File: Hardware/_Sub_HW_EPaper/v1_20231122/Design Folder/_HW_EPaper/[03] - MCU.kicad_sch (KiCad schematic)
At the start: 7 parts, among them J301 HDR_4POS_VERT, U301 PIC16F15223_8BIT

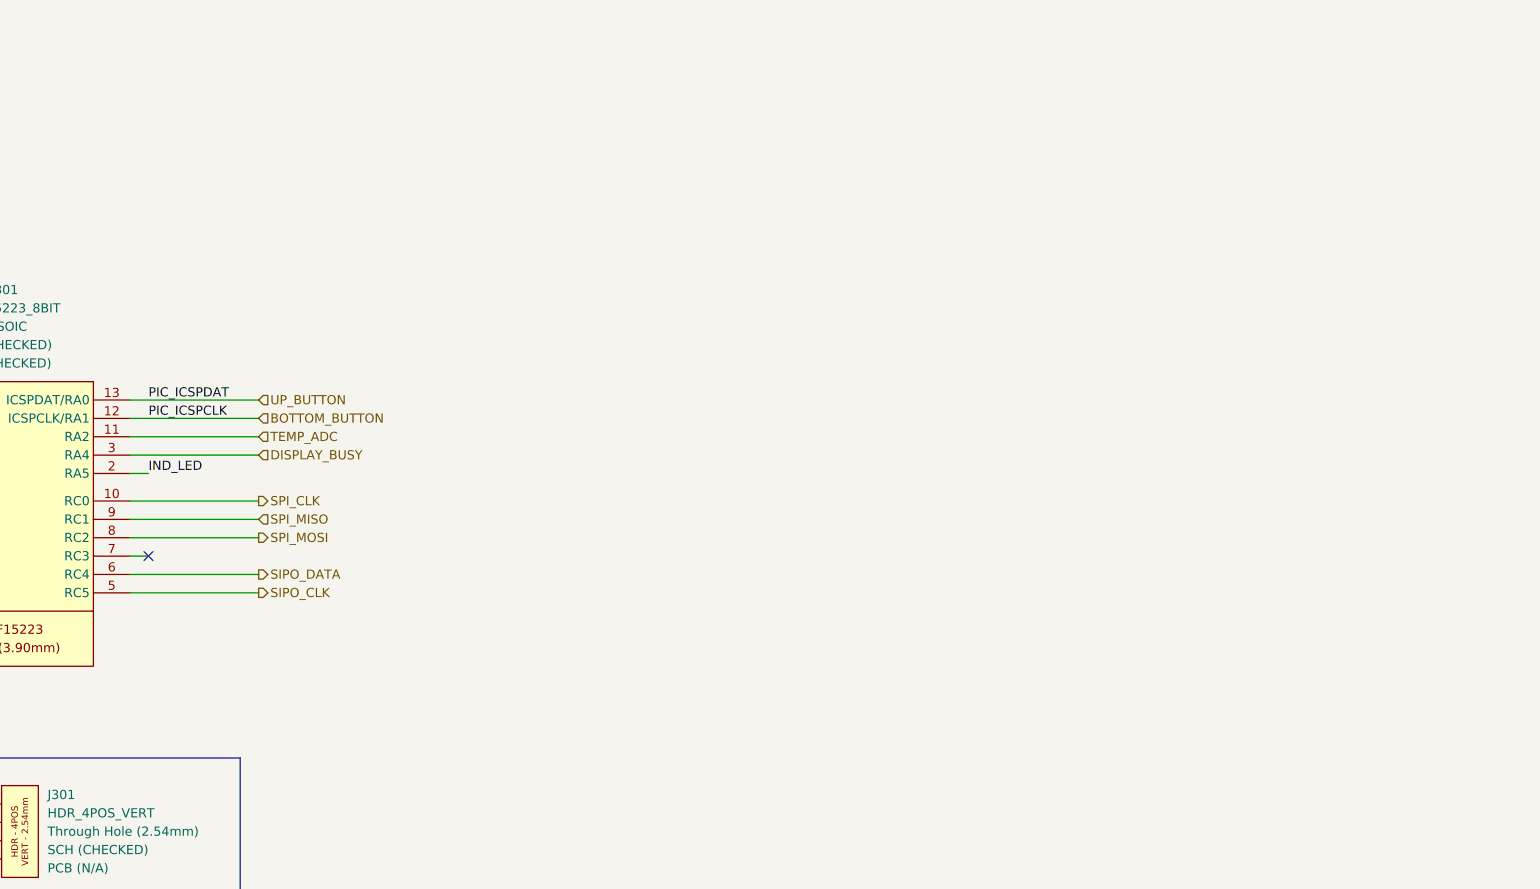
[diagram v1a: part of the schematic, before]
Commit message: Working on epaper hardware
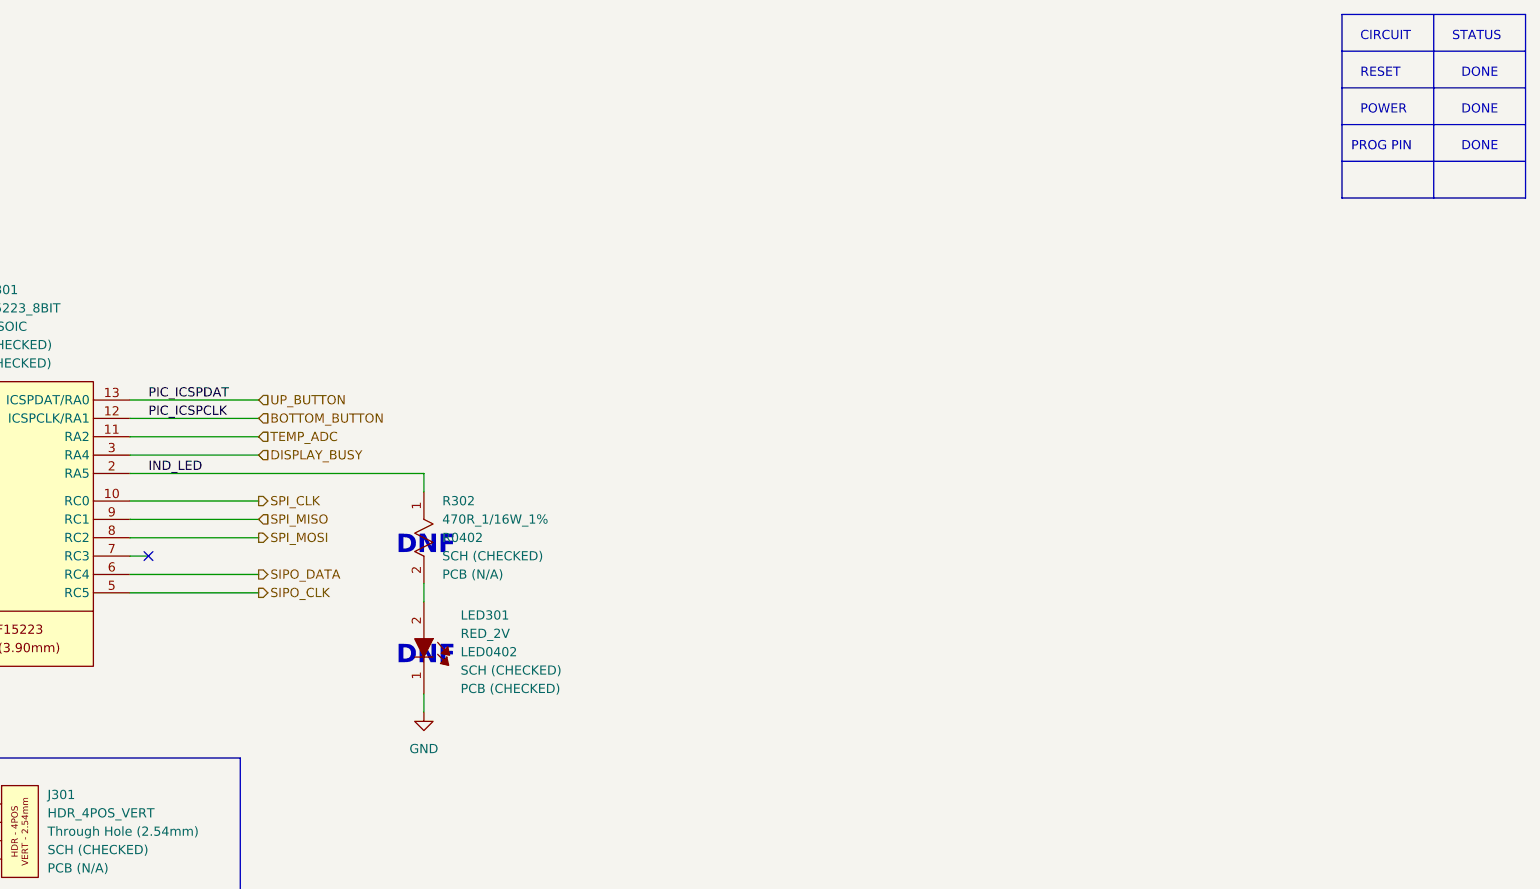
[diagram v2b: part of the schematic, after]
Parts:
- added LED301: RED_2V, LED_SMD:LED_0402_1005Metric, symbol _SCHLIB_Epaper:LED_RED_2V_624nm_LED0402
- added R302: 470R_1/16W_1%, Resistor_SMD:R_0402_1005Metric, symbol _SCHLIB_Epaper:RES_470R_1/16W_1%_R0402
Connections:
- net GND: now also LED301.1
- net IND_LED: now also R302.1
- new net: LED301.2, R302.2
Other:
- note added: "CIRCUIT"
- note added: "DNF"
- note added: "DONE"
- note added: "POWER"
- note added: "PROG PIN"
- note added: "RESET"
- note added: "STATUS"
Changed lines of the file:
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@@
     (company "Mend0z0")
     (comment 1 "v1.0")
-    (comment 2 "PRELIMINARY")
+    (comment 2 "CHECKED")
   )
   (junction (at 135.89 128.27) (diameter 0) (color 0 0 0 0)
@@
     (stroke (width 0) (type default))
   )
+  (wire (pts (xy 254 129.54) (xy 254 132.08))
+    (stroke (width 0) (type default))
+  )
   (wire (pts (xy 156.21 128.27) (xy 156.21 130.81))
     (stroke (width 0) (type default))
@@
     (stroke (width 0) (type default))
   )
+  (polyline (pts (xy 381 60.96) (xy 406.4 60.96))
+    (stroke (width 0) (type default))
+  )
   (wire (pts (xy 135.89 102.87) (xy 135.89 104.14))
     (stroke (width 0) (type default))
@@
     (stroke (width 0) (type default))
   )
+  (polyline (pts (xy 393.7 50.8) (xy 393.7 76.2))
+    (stroke (width 0) (type default))
+  )
   (wire (pts (xy 213.36 106.68) (xy 231.14 106.68))
     (stroke (width 0) (type default))
   )
-  (wire (pts (xy 213.36 114.3) (xy 215.9 114.3))
+  (wire (pts (xy 213.36 114.3) (xy 254 114.3))
     (stroke (width 0) (type default))
   )
@@
     (stroke (width 0) (type default))
   )
+  (polyline (pts (xy 381 55.88) (xy 406.4 55.88))
+    (stroke (width 0) (type default))
+  )
   (wire (pts (xy 135.89 130.81) (xy 135.89 128.27))
     (stroke (width 0) (type default))
@@
     (stroke (width 0) (type default))
   )
+  (wire (pts (xy 254 147.32) (xy 254 144.78))
+    (stroke (width 0) (type default))
+  )
   (wire (pts (xy 231.14 130.81) (xy 213.36 130.81))
     (stroke (width 0) (type default))
@@
     (stroke (width 0) (type default))
   )
+  (wire (pts (xy 254 116.84) (xy 254 114.3))
+    (stroke (width 0) (type default))
+  )
   (wire (pts (xy 177.8 130.81) (xy 175.26 130.81))
     (stroke (width 0) (type default))
@@
     (stroke (width 0) (type default))
   )
+  (polyline (pts (xy 381 71.12) (xy 406.4 71.12))
+    (stroke (width 0) (type default))
+  )
   (polyline (pts (xy 109.22 140.97) (xy 134.62 129.54))
     (stroke (width 0) (type default))
@@
     (stroke (width 0) (type default))
   )
+  (polyline (pts (xy 381 66.04) (xy 406.4 66.04))
+    (stroke (width 0) (type default))
+  )
   (rectangle (start 69.85 99.06) (end 110.49 110.49)
     (stroke (width 0) (type default))
     (fill (type none))
   )
+  (rectangle (start 381 50.8) (end 406.4 76.2)
+    (stroke (width 0) (type default))
+    (fill (type none))
+  )
   (circle (center 135.89 128.27) (radius 1.27)
     (stroke (width 0) (type default))
@@
   )
   (text "HPF1" (at 137.16 127 0)
+    (effects (font (size 1.27 1.27)) (justify left bottom))
+  )
+  (text "RESET" (at 383.54 59.69 0)
+    (effects (font (size 1.27 1.27)) (justify left bottom))
+  )
+  (text "DNF" (at 250.19 125.73 0)
+    (effects (font (size 2.54 2.54) (thickness 0.508) bold) (justify left bottom))
+  )
+  (text "DONE" (at 397.51 64.77 0)
     (effects (font (size 1.27 1.27)) (justify left bottom))
   )
@@
     (effects (font (size 2 2) (thickness 0.4) bold) (justify left bottom))
   )
+  (text "PROG PIN" (at 382.27 69.85 0)
+    (effects (font (size 1.27 1.27)) (justify left bottom))
+  )
+  (text "POWER" (at 383.54 64.77 0)
+    (effects (font (size 1.27 1.27)) (justify left bottom))
+  )
+  (text "DONE" (at 397.51 59.69 0)
+    (effects (font (size 1.27 1.27)) (justify left bottom))
+  )
+  (text "DONE" (at 397.51 69.85 0)
+    (effects (font (size 1.27 1.27)) (justify left bottom))
+  )
   (text "HPF: 1/(10*10^3 * 1*10^-6) = 1 kHz" (at 71.12 107.95 0)
     (effects (font (size 1.27 1.27)) (justify left bottom))
@@
     (effects (font (size 1.27 1.27)) (justify left bottom))
   )
+  (text "DNF" (at 250.19 140.97 0)
+    (effects (font (size 2.54 2.54) (thickness 0.508) bold) (justify left bottom))
+  )
+  (text "STATUS" (at 396.24 54.61 0)
+    (effects (font (size 1.27 1.27)) (justify left bottom))
+  )
   (text "PROGRAMMER PINS\n\n" (at 179.07 181.61 0)
     (effects (font (size 2.54 2.54)) (justify left bottom))
   )
+  (text "CIRCUIT" (at 383.54 54.61 0)
+    (effects (font (size 1.27 1.27)) (justify left bottom))
+  )
   (label "PIC_ICSPDAT" (at 176.53 165.1 0) (fields_autoplaced)
     (effects (font (size 1.27 1.27)) (justify left bottom))
@@
   (hierarchical_label "VIN" (shape input) (at 133.35 87.63 180) (fields_autoplaced)
     (effects (font (size 1.27 1.27)) (justify right))
+  )
+  (symbol (lib_id "_SCHLIB_Epaper:RES_470R_1/16W_1%_R0402") (at 254 116.84 270) (unit 1)
+    (in_bom yes) (on_board yes) (dnp no) (fields_autoplaced)
+    (property "Reference" "R302" (at 256.54 118.11 90)
+      (effects (font (size 1.27 1.27)) (justify left))
+    )
+    (property "Value" "470R_1/16W_1%" (at 256.54 120.65 90)
+      (effects (font (size 1.27 1.27)) (justify left))
+    )
+    (property "Footprint" "Resistor_SMD:R_0402_1005Metric" (at 270.51 119.38 0)
+      (effects (font (size 1.27 1.27)) (justify left) hide)
+    )
+    (property "Datasheet" "https://www.bourns.com/docs/product-datasheets/cr.pdf?sfvrsn=574d41f6_14" (at 262.89 119.38 0)
+      (effects (font (size 1.27 1.27)) (justify left) hide)
+    )
+    (property "Description" "470 Ohms ±1% 0.063W, 1/16W Chip Resistor 0402 (1005 Metric) Thick Film" (at 267.97 119.38 0)
+      (effects (font (size 1.27 1.27)) (justify left) hide)
+    )
+    (property "Part Number" "CR0402-FX-4700GLF" (at 273.05 119.38 0)
+      (effects (font (size 1.27 1.27)) (justify left) hide)
+    )
+    (property "Link" "https://www.digikey.ca/en/products/detail/bourns-inc/CR0402-FX-4700GLF/3783391" (at 265.43 119.38 0)
+      (effects (font (size 1.27 1.27)) (justify left) hide)
+    )
+    (property "Package" "R0402" (at 256.54 123.19 90)
+      (effects (font (size 1.27 1.27)) (justify left))
+    )
+    (property "SCH CHECK" "SCH (CHECKED)" (at 256.54 125.73 90)
+      (effects (font (size 1.27 1.27)) (justify left))
+    )
+    (property "PCB CHECK" "PCB (N/A)" (at 256.54 128.27 90)
+      (effects (font (size 1.27 1.27)) (justify left))
+    )
+    (pin "1")
+    (pin "2")
+    (instances
+      (project "_HW_EPaper"
+        (path "/adfaa0ae-c952-44c7-bc24-1bfe8f9a84a3/4e346fc8-747a-4f3e-83e0-81c9211edb38/99cad234-6d2d-4b92-87e6-f4f0e962eb13"
+          (reference "R302") (unit 1)
+        )
+      )
+    )
   )
   (symbol (lib_id "_SCHLIB_Epaper:MCU_PIC16F15223-E/SL_8BIT_14-SOIC") (at 182.88 101.6 0) (unit 1)
@@
     )
   )
+  (symbol (lib_id "power:GND") (at 254 147.32 0) (unit 1)
+    (in_bom yes) (on_board yes) (dnp no) (fields_autoplaced)
+    (property "Reference" "#PWR0302" (at 254 153.67 0)
+      (effects (font (size 1.27 1.27)) hide)
+    )
+    (property "Value" "GND" (at 254 152.4 0)
+      (effects (font (size 1.27 1.27)))
+    )
+    (property "Footprint" "" (at 254 147.32 0)
+      (effects (font (size 1.27 1.27)) hide)
+    )
+    (property "Datasheet" "" (at 254 147.32 0)
+      (effects (font (size 1.27 1.27)) hide)
+    )
+    (pin "1")
+    (instances
+      (project "[03] - MCU"
+        (path "/9bbd5852-431d-48c8-bae6-0765e432421a"
+          (reference "#PWR0302") (unit 1)
+        )
+      )
+      (project "_HW_EPen"
+        (path "/9ee621ae-6984-4881-898c-f5f3c9433407/7dba9ac4-cfde-4903-b774-f23f20ffdff2/4f69a756-13f1-41da-a917-ef791025fd7a"
+          (reference "#PWR0302") (unit 1)
+        )
+      )
+      (project "_HW_EPaper"
+        (path "/adfaa0ae-c952-44c7-bc24-1bfe8f9a84a3/4e346fc8-747a-4f3e-83e0-81c9211edb38/99cad234-6d2d-4b92-87e6-f4f0e962eb13"
+          (reference "#PWR0303") (unit 1)
+        )
+      )
+    )
+  )
+  (symbol (lib_id "_SCHLIB_Epaper:LED_RED_2V_624nm_LED0402") (at 254 132.08 270) (unit 1)
+    (in_bom yes) (on_board yes) (dnp no) (fields_autoplaced)
+    (property "Reference" "LED301" (at 259.08 133.9215 90)
+      (effects (font (size 1.27 1.27)) (justify left))
+    )
+    (property "Value" "RED_2V" (at 259.08 136.4615 90)
+      (effects (font (size 1.27 1.27)) (justify left))
+    )
+    (property "Footprint" "LED_SMD:LED_0402_1005Metric" (at 273.05 134.62 0)
+      (effects (font (size 1.27 1.27)) (justify left) hide)
+    )
+    (property "Datasheet" "https://media.digikey.com/pdf/Data%20Sheets/Harvatek%20PDFs/B2841USD-20D001014U1930.pdf" (at 265.43 134.62 0)
+      (effects (font (size 1.27 1.27)) (justify left) hide)
+    )
+    (property "Description" "Red 624nm LED Indication - Discrete 2V 0402 (1005 Metric)" (at 270.51 134.62 0)
+      (effects (font (size 1.27 1.27)) (justify left) hide)
+    )
+    (property "Part Number" "B2841USD-20D001014U1930" (at 275.59 134.62 0)
+      (effects (font (size 1.27 1.27)) (justify left) hide)
+    )
+    (property "Link" "https://www.digikey.ca/en/products/detail/harvatek-corporation/B2841USD-20D001014U1930/16729514?s=N4IgTCBcDaIEJgBwBYCMBVAygEQLRgAZsCDVTl1UBOAZgJAF0BfIA" (at 267.97 134.62 0)
+      (effects (font (size 1.27 1.27)) (justify left) hide)
+    )
+    (property "Package" "LED0402" (at 259.08 139.0015 90)
+      (effects (font (size 1.27 1.27)) (justify left))
+    )
+    (property "SCH CHECK" "SCH (CHECKED)" (at 259.08 141.5415 90)
+      (effects (font (size 1.27 1.27)) (justify left))
+    )
+    (property "PCB CHECK" "PCB (CHECKED)" (at 259.08 144.0815 90)
+      (effects (font (size 1.27 1.27)) (justify left))
+    )
+    (pin "2")
+    (pin "1")
+    (instances
+      (project "_HW_EPaper"
+        (path "/adfaa0ae-c952-44c7-bc24-1bfe8f9a84a3/4e346fc8-747a-4f3e-83e0-81c9211edb38/99cad234-6d2d-4b92-87e6-f4f0e962eb13"
+          (reference "LED301") (unit 1)
+        )
+      )
+    )
+  )
   (symbol (lib_id "_SCHLIB_Epaper:CAP_100nF_50V_X7R_C0402") (at 156.21 130.81 270) (unit 1)
     (in_bom yes) (on_board yes) (dnp no) (fields_autoplaced)
@@
       (project "_HW_EPaper"
         (path "/adfaa0ae-c952-44c7-bc24-1bfe8f9a84a3/4e346fc8-747a-4f3e-83e0-81c9211edb38/99cad234-6d2d-4b92-87e6-f4f0e962eb13"
-          (reference "R304") (unit 1)
-        )
-      )
+          (reference "R303") (unit 1)
+        )
+      )

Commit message: Updating file templates and structures...
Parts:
- C301, C303: Manufacturer (none) -> Murata Electronics; Part Number GRM155R71H104KE14J -> (none); Part Number (Manufacturer) (none) -> GRM155R71H104KE14J; Part Number (Vendor) (none) -> 490-13342-2-ND; Vendor (none) -> Digikey
- C302: Manufacturer (none) -> Murata Electronics; Part Number GRM155Z71A105KE01D -> (none); Part Number (Manufacturer) (none) -> GRM155Z71A105KE01D; Part Number (Vendor) (none) -> 490-GRM155Z71A105KE01DTR-ND; Vendor (none) -> Digikey
- J301: Manufacturer (none) -> Adam Tech; Part Number PH1-04-UA -> (none); Part Number (Manufacturer) (none) -> PH1-04-UA; Part Number (Vendor) (none) -> 2057-PH1-04-UA-ND; Vendor (none) -> Digikey
- LED301: Manufacturer (none) -> Harvatek Corporation; Part Number B2841USD-20D001014U1930 -> (none); Part Number (Manufacturer) (none) -> B2841USD-20D001014U1930; Part Number (Vendor) (none) -> 3147-B2841USD-20D001014U1930TR-ND; Vendor (none) -> Digikey
- R301: Manufacturer (none) -> Bourns Inc.; Part Number CR0402-FX-1002GLF -> (none); Part Number (Manufacturer) (none) -> CR0402-FX-1002GLF; Part Number (Vendor) (none) -> CR0402-FX-1002GLFTR-ND; Vendor (none) -> Digikey
- R302: Manufacturer (none) -> Bourns Inc.; Part Number CR0402-FX-4700GLF -> (none); Part Number (Manufacturer) (none) -> CR0402-FX-4700GLF; Part Number (Vendor) (none) -> CR0402-FX-4700GLFTR-ND; Vendor (none) -> Digikey
- R302: Manufacturer (none) -> Stackpole Electronics Inc; Part Number RNCP0805FTD1R00 -> (none); Part Number (Manufacturer) (none) -> RNCP0805FTD1R00; Part Number (Vendor) (none) -> RNCP0805FTD1R00TR-ND; Vendor (none) -> Digikey
- U301: Manufacturer (none) -> Microchip Technology; Part Number PIC16F15223-E/SL -> (none); Part Number (Manufacturer) (none) -> PIC16F15223-E/SL; Part Number (Vendor) (none) -> 150-PIC16F15223-E/SL-ND; Vendor (none) -> Digikey
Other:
- moved on the sheet: C301, C302, C303, J301, LED301, R301, R302, U301
